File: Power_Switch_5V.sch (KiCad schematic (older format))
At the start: 6 parts

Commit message: assign footprint
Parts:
- D?: footprint (none) -> LEDs:LED_0603
- JP?: footprint (none) -> Pin_Headers:Pin_Header_Straight_1x02_Pitch2.00mm
- P?: footprint (none) -> auv:XT60
- R?: footprint (none) -> Resistors_SMD:R_0603
- U?: footprint (none) -> auv:TEN_20WIN
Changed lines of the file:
@@
 F 0 "U?" H 5150 4050 60  0000 C CNN
 F 1 "TEN_20-2411WIN" H 5500 3300 60  0000 C CNN
-F 2 "" H 5500 3600 60  0000 C CNN
+F 2 "auv:TEN_20WIN" H 5450 3200 60  0000 C CNN
 F 3 "" H 5500 3600 60  0000 C CNN
 	1    5450 3700
@@
 F 0 "R?" V 6530 3800 50  0000 C CNN
 F 1 "R" V 6450 3800 50  0000 C CNN
-F 2 "" V 6380 3800 50  0001 C CNN
+F 2 "Resistors_SMD:R_0603" V 6380 3800 50  0001 C CNN
 F 3 "" H 6450 3800 50  0001 C CNN
 	1    6450 3800
@@
 F 0 "D?" H 6400 4325 50  0000 L CNN
 F 1 "LED_Small" H 6275 4100 50  0000 L CNN
-F 2 "" V 6450 4200 50  0001 C CNN
+F 2 "LEDs:LED_0603" V 6450 4200 50  0001 C CNN
 F 3 "" V 6450 4200 50  0001 C CNN
 	1    6450 4200
@@
 F 0 "P?" H 7050 4150 50  0000 C CNN
 F 1 "XT60" H 7050 3850 50  0000 C CNN
-F 2 "" H 7050 4000 60  0000 C CNN
+F 2 "auv:XT60" H 7150 3750 60  0000 C CNN
 F 3 "" H 7050 4000 60  0000 C CNN
 	1    7050 4000
@@
 F 0 "JP?" H 4400 4100 50  0000 C CNN
 F 1 "Jumper" H 4400 3870 50  0000 C CNN
-F 2 "" H 4400 3950 50  0001 C CNN
+F 2 "Pin_Headers:Pin_Header_Straight_1x02_Pitch2.00mm" H 4400 3950 50  0001 C CNN
 F 3 "" H 4400 3950 50  0001 C CNN
 	1    4400 3950

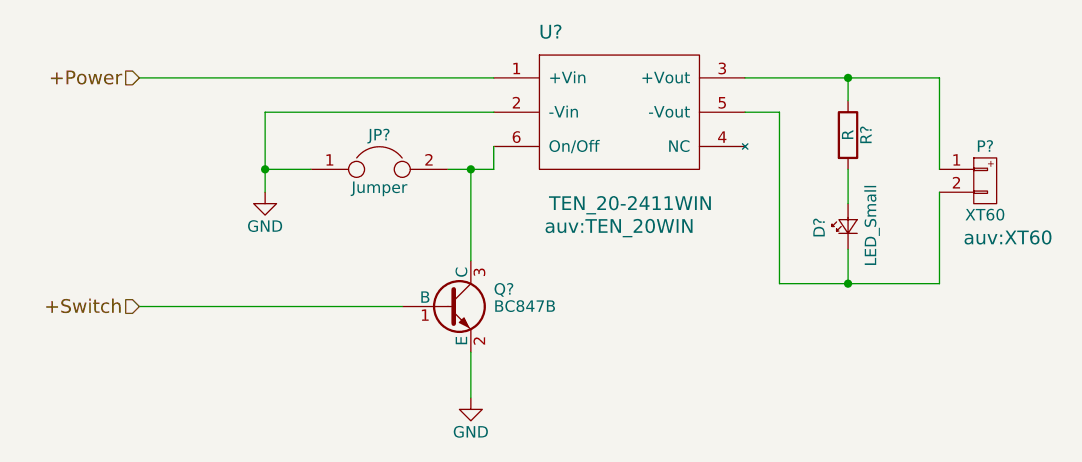
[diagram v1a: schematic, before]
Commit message: add R at base of BJT
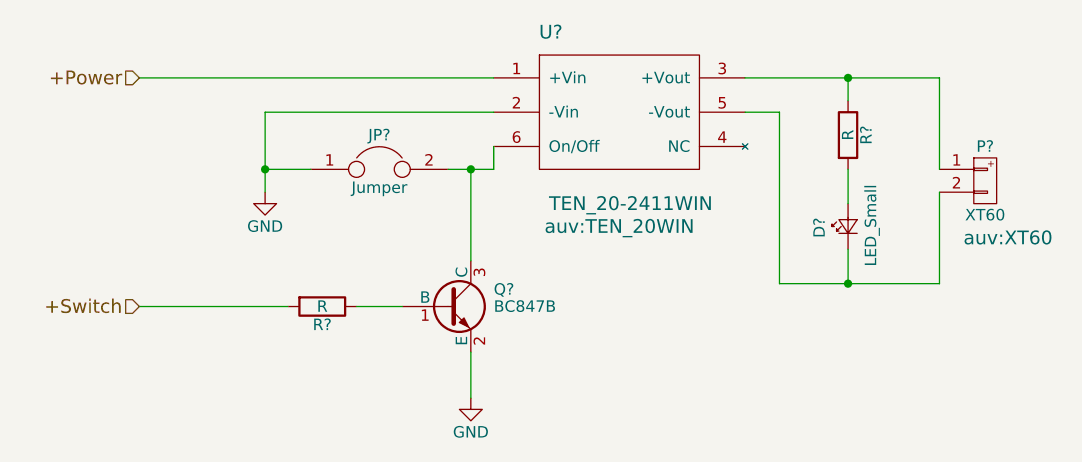
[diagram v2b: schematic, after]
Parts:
- added R?: R, Resistors_SMD:R_0603, symbol R
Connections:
- net +Switch: now also R?.2; no longer Q?.1 (B)
- new net: Q?.1 (B), R?.1
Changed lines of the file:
@@
 +Switch
 Wire Wire Line
-	3350 4550 4500 4550
+	3350 3550 4900 3550
+$Comp
+L R R?
+U 1 1 58E00964
+P 4150 4550
+F 0 "R?" V 4230 4550 50  0000 C CNN
+F 1 "R" V 4150 4550 50  0000 C CNN
+F 2 "Resistors_SMD:R_0603" V 4080 4550 50  0001 C CNN
+F 3 "" H 4150 4550 50  0001 C CNN
+	1    4150 4550
+	0    1    1    0
+$EndComp
 Wire Wire Line
-	3350 3550 4900 3550
+	4500 4550 4300 4550
+Wire Wire Line
+	4000 4550 3350 4550
 $EndSCHEMATC
